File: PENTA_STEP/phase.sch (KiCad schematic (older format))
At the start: 12 parts, among them Q1 BUK9K45-100E,115, Q2 BUK9K45-100E,115

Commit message: V1 layout nearing completion
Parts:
- C27, C28, C29: footprint Capacitor_SMD:C_0603_1608Metric -> Capacitor_SMD:C_0603_1608Metric_Pad1.05x0.95mm_HandSolder
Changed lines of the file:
@@
 AR Path="/5F24B60D/5E4B900F/5E30367B" Ref="Q17"  Part="1"
 AR Path="/5F24B60D/5E4B9032/5E30367B" Ref="Q19"  Part="1"
-F 0 "Q19" H 5400 3000 50  0000 L CNN
+F 0 "Q1" H 5400 3000 50  0000 L CNN
 F 1 "BUK9K45-100E,115" H 5487 2905 50  0001 L CNN
 F 2 "CUSTOM_FP:TRANS_BUK7K12-60EX" H 5400 2875 50  0001 L CIN
@@
 AR Path="/5F24B60D/5E4B900F/5E303682" Ref="Q18"  Part="1"
 AR Path="/5F24B60D/5E4B9032/5E303682" Ref="Q20"  Part="1"
-F 0 "Q20" H 6300 3000 50  0000 L CNN
+F 0 "Q2" H 6300 3000 50  0000 L CNN
 F 1 "BUK9K45-100E,115" H 6388 2905 50  0001 L CNN
 F 2 "CUSTOM_FP:TRANS_BUK7K12-60EX" H 6300 2875 50  0001 L CIN
@@
 AR Path="/5F24B60D/5E4B900F/5E303689" Ref="Q17"  Part="2"
 AR Path="/5F24B60D/5E4B9032/5E303689" Ref="Q19"  Part="2"
-F 0 "Q19" H 5400 4250 50  0000 L CNN
+F 0 "Q1" H 5400 4250 50  0000 L CNN
 F 1 "BUK9K45-100E,115" H 5487 4155 50  0001 L CNN
 F 2 "CUSTOM_FP:TRANS_BUK7K12-60EX" H 5400 4125 50  0001 L CIN
@@
 AR Path="/5F24B60D/5E4B900F/5E303690" Ref="Q18"  Part="2"
 AR Path="/5F24B60D/5E4B9032/5E303690" Ref="Q20"  Part="2"
-F 0 "Q20" H 6300 4250 50  0000 L CNN
+F 0 "Q2" H 6300 4250 50  0000 L CNN
 F 1 "BUK9K45-100E,115" H 6388 4155 50  0001 L CNN
 F 2 "CUSTOM:TRANS_BUK7K12-60EX" H 6300 4125 50  0001 L CIN
@@
 AR Path="/5F24B60D/5E4B900F/5E303697" Ref="#PWR0109"  Part="1"
 AR Path="/5F24B60D/5E4B9032/5E303697" Ref="#PWR0111"  Part="1"
-F 0 "#PWR0111" H 5650 4950 50  0001 C CNN
+F 0 "#PWR043" H 5650 4950 50  0001 C CNN
 F 1 "GND" H 5650 5100 50  0000 C TNN
 F 2 "" H 5650 5200 50  0001 C CNN
@@
 AR Path="/5F24B60D/5E4B900F/5E30369F" Ref="R17"  Part="1"
 AR Path="/5F24B60D/5E4B9032/5E30369F" Ref="R24"  Part="1"
-F 0 "R24" V 5550 4850 50  0000 C CNN
+F 0 "R95" V 5550 4850 50  0000 C CNN
 F 1 "0R022" V 5750 4850 50  0000 C CNN
 F 2 "CUSTOM_FP:WSH2818R0500FEA" V 5580 4850 50  0001 C CNN
@@
 AR Path="/5F24B60D/5E4B900F/5E3036A9" Ref="R14"  Part="1"
 AR Path="/5F24B60D/5E4B9032/5E3036A9" Ref="R21"  Part="1"
-F 0 "R21" V 4700 4200 50  0000 C CNN
+F 0 "R92" V 4700 4200 50  0000 C CNN
 F 1 "22R" V 4900 4200 50  0000 C CNN
 F 2 "Resistor_SMD:R_0603_1608Metric_Pad1.05x0.95mm_HandSolder" V 4730 4200 50  0001 C CNN
@@
 AR Path="/5F24B60D/5E4B900F/5E3036B3" Ref="R19"  Part="1"
 AR Path="/5F24B60D/5E4B9032/5E3036B3" Ref="R26"  Part="1"
-F 0 "R26" V 6400 4200 50  0000 C CNN
+F 0 "R97" V 6400 4200 50  0000 C CNN
 F 1 "22R" V 6600 4200 50  0000 C CNN
 F 2 "Resistor_SMD:R_0603_1608Metric_Pad1.05x0.95mm_HandSolder" V 6430 4200 50  0001 C CNN
@@
 AR Path="/5F24B60D/5E4B900F/5E3036BD" Ref="R18"  Part="1"
 AR Path="/5F24B60D/5E4B9032/5E3036BD" Ref="R25"  Part="1"
-F 0 "R25" V 6400 2950 50  0000 C CNN
+F 0 "R96" V 6400 2950 50  0000 C CNN
 F 1 "22R" V 6600 2950 50  0000 C CNN
 F 2 "Resistor_SMD:R_0603_1608Metric_Pad1.05x0.95mm_HandSolder" V 6430 2950 50  0001 C CNN
@@
 AR Path="/5F24B60D/5E4B900F/5E3036C7" Ref="R13"  Part="1"
 AR Path="/5F24B60D/5E4B9032/5E3036C7" Ref="R20"  Part="1"
-F 0 "R20" V 4700 2950 50  0000 C CNN
+F 0 "R91" V 4700 2950 50  0000 C CNN
 F 1 "22R" V 4900 2950 50  0000 C CNN
 F 2 "Resistor_SMD:R_0603_1608Metric_Pad1.05x0.95mm_HandSolder" V 4730 2950 50  0001 C CNN
@@
 AR Path="/5F24B60D/5E4B900F/5E3036D1" Ref="R15"  Part="1"
 AR Path="/5F24B60D/5E4B9032/5E3036D1" Ref="R22"  Part="1"
-F 0 "R22" V 5000 4650 50  0000 C CNN
+F 0 "R93" V 5000 4650 50  0000 C CNN
 F 1 "47R" V 5200 4650 50  0000 C CNN
 F 2 "Resistor_SMD:R_0603_1608Metric_Pad1.05x0.95mm_HandSolder" V 5030 4650 50  0001 C CNN
@@
 AR Path="/5F24B60D/5E4B900F/5E3036DB" Ref="R16"  Part="1"
 AR Path="/5F24B60D/5E4B9032/5E3036DB" Ref="R23"  Part="1"
-F 0 "R23" V 5000 5050 50  0000 C CNN
+F 0 "R94" V 5000 5050 50  0000 C CNN
 F 1 "47R" V 5200 5050 50  0000 C CNN
 F 2 "Resistor_SMD:R_0603_1608Metric_Pad1.05x0.95mm_HandSolder" V 5030 5050 50  0001 C CNN
@@
 AR Path="/5F24B60D/5E4B900F/5E3036E5" Ref="C97"  Part="1"
 AR Path="/5F24B60D/5E4B9032/5E3036E5" Ref="C100"  Part="1"
-F 0 "C100" H 6265 2346 50  0000 L CNN
+F 0 "C29" H 6265 2346 50  0000 L CNN
 F 1 "470n" H 6265 2255 50  0000 L CNN
-F 2 "Capacitor_SMD:C_0603_1608Metric" H 6188 2150 50  0001 C CNN
+F 2 "Capacitor_SMD:C_0603_1608Metric_Pad1.05x0.95mm_HandSolder" H 6188 2150 50  0001 C CNN
 F 3 "~" H 6150 2300 50  0001 C CNN
 F 4 "885012106008" H 6150 2300 50  0001 C CNN "MPN"
@@
 AR Path="/5F24B60D/5E4B900F/5E3036EF" Ref="C95"  Part="1"
 AR Path="/5F24B60D/5E4B9032/5E3036EF" Ref="C98"  Part="1"
-F 0 "C98" V 5000 3450 50  0000 L BNN
+F 0 "C27" V 5000 3450 50  0000 L BNN
 F 1 "220n" V 5000 3350 50  0000 R BNN
-F 2 "Capacitor_SMD:C_0603_1608Metric" H 5038 3250 50  0001 C CNN
+F 2 "Capacitor_SMD:C_0603_1608Metric_Pad1.05x0.95mm_HandSolder" H 5038 3250 50  0001 C CNN
 F 3 "~" H 5000 3400 50  0001 C CNN
 F 4 "CL10F224ZB8NNNC" H 5000 3400 50  0001 C CNN "MPN"
@@
 AR Path="/5F24B60D/5E4B900F/5E303702" Ref="C96"  Part="1"
 AR Path="/5F24B60D/5E4B9032/5E303702" Ref="C99"  Part="1"
-F 0 "C99" V 5000 3650 50  0000 L BNN
+F 0 "C28" V 5000 3650 50  0000 L BNN
 F 1 "220n" V 5000 3550 50  0000 R BNN
-F 2 "Capacitor_SMD:C_0603_1608Metric" H 5038 3450 50  0001 C CNN
+F 2 "Capacitor_SMD:C_0603_1608Metric_Pad1.05x0.95mm_HandSolder" H 5038 3450 50  0001 C CNN
 F 3 "~" H 5000 3600 50  0001 C CNN
 F 4 "CL10F224ZB8NNNC" H 5000 3600 50  0001 C CNN "MPN"
@@
 AR Path="/5F24B60D/5E4B900F/5E303736" Ref="#PWR0110"  Part="1"
 AR Path="/5F24B60D/5E4B9032/5E303736" Ref="#PWR0112"  Part="1"
-F 0 "#PWR0112" H 6150 2250 50  0001 C CNN
+F 0 "#PWR044" H 6150 2250 50  0001 C CNN
 F 1 "GND" H 6150 2400 50  0000 C TNN
 F 2 "" H 6150 2500 50  0001 C CNN

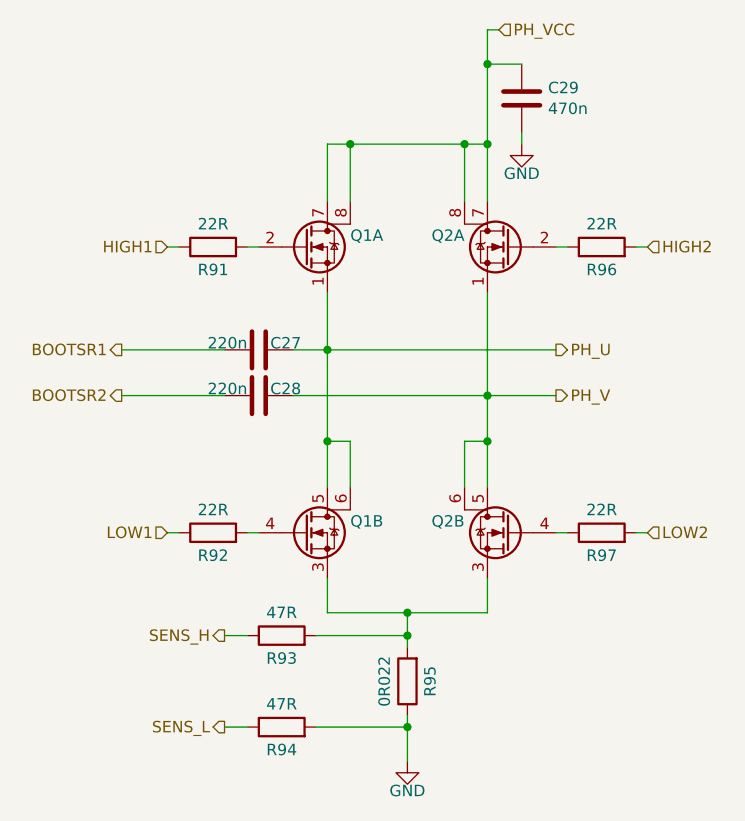
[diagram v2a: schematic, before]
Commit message: Added two FET-controlled outputs to the board
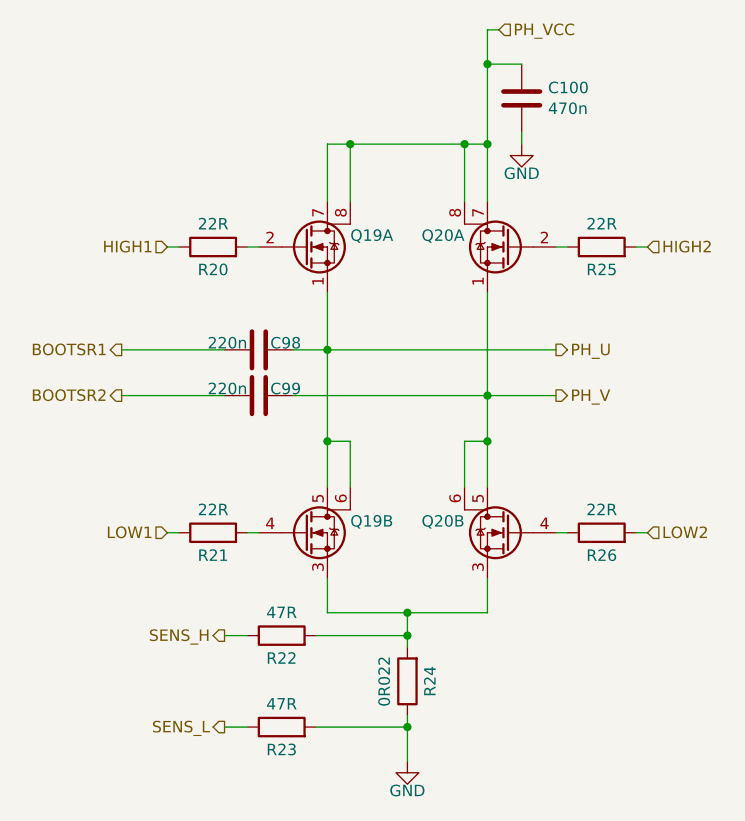
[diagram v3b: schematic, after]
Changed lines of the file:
@@
 AR Path="/5F24B60D/5E4B900F/5E30367B" Ref="Q17"  Part="1"
 AR Path="/5F24B60D/5E4B9032/5E30367B" Ref="Q19"  Part="1"
-F 0 "Q1" H 5400 3000 50  0000 L CNN
+F 0 "Q19" H 5400 3000 50  0000 L CNN
 F 1 "BUK9K45-100E,115" H 5487 2905 50  0001 L CNN
 F 2 "CUSTOM_FP:TRANS_BUK7K12-60EX" H 5400 2875 50  0001 L CIN
@@
 AR Path="/5F24B60D/5E4B900F/5E303682" Ref="Q18"  Part="1"
 AR Path="/5F24B60D/5E4B9032/5E303682" Ref="Q20"  Part="1"
-F 0 "Q2" H 6300 3000 50  0000 L CNN
+F 0 "Q20" H 6300 3000 50  0000 L CNN
 F 1 "BUK9K45-100E,115" H 6388 2905 50  0001 L CNN
 F 2 "CUSTOM_FP:TRANS_BUK7K12-60EX" H 6300 2875 50  0001 L CIN
@@
 AR Path="/5F24B60D/5E4B900F/5E303689" Ref="Q17"  Part="2"
 AR Path="/5F24B60D/5E4B9032/5E303689" Ref="Q19"  Part="2"
-F 0 "Q1" H 5400 4250 50  0000 L CNN
+F 0 "Q19" H 5400 4250 50  0000 L CNN
 F 1 "BUK9K45-100E,115" H 5487 4155 50  0001 L CNN
 F 2 "CUSTOM_FP:TRANS_BUK7K12-60EX" H 5400 4125 50  0001 L CIN
@@
 AR Path="/5F24B60D/5E4B900F/5E303690" Ref="Q18"  Part="2"
 AR Path="/5F24B60D/5E4B9032/5E303690" Ref="Q20"  Part="2"
-F 0 "Q2" H 6300 4250 50  0000 L CNN
+F 0 "Q20" H 6300 4250 50  0000 L CNN
 F 1 "BUK9K45-100E,115" H 6388 4155 50  0001 L CNN
 F 2 "CUSTOM:TRANS_BUK7K12-60EX" H 6300 4125 50  0001 L CIN
@@
 AR Path="/5F24B60D/5E4B900F/5E303697" Ref="#PWR0109"  Part="1"
 AR Path="/5F24B60D/5E4B9032/5E303697" Ref="#PWR0111"  Part="1"
-F 0 "#PWR043" H 5650 4950 50  0001 C CNN
+F 0 "#PWR0111" H 5650 4950 50  0001 C CNN
 F 1 "GND" H 5650 5100 50  0000 C TNN
 F 2 "" H 5650 5200 50  0001 C CNN
@@
 AR Path="/5F24B60D/5E4B900F/5E30369F" Ref="R17"  Part="1"
 AR Path="/5F24B60D/5E4B9032/5E30369F" Ref="R24"  Part="1"
-F 0 "R95" V 5550 4850 50  0000 C CNN
+F 0 "R24" V 5550 4850 50  0000 C CNN
 F 1 "0R022" V 5750 4850 50  0000 C CNN
 F 2 "CUSTOM_FP:WSH2818R0500FEA" V 5580 4850 50  0001 C CNN
@@
 AR Path="/5F24B60D/5E4B900F/5E3036A9" Ref="R14"  Part="1"
 AR Path="/5F24B60D/5E4B9032/5E3036A9" Ref="R21"  Part="1"
-F 0 "R92" V 4700 4200 50  0000 C CNN
+F 0 "R21" V 4700 4200 50  0000 C CNN
 F 1 "22R" V 4900 4200 50  0000 C CNN
 F 2 "Resistor_SMD:R_0603_1608Metric_Pad1.05x0.95mm_HandSolder" V 4730 4200 50  0001 C CNN
@@
 AR Path="/5F24B60D/5E4B900F/5E3036B3" Ref="R19"  Part="1"
 AR Path="/5F24B60D/5E4B9032/5E3036B3" Ref="R26"  Part="1"
-F 0 "R97" V 6400 4200 50  0000 C CNN
+F 0 "R26" V 6400 4200 50  0000 C CNN
 F 1 "22R" V 6600 4200 50  0000 C CNN
 F 2 "Resistor_SMD:R_0603_1608Metric_Pad1.05x0.95mm_HandSolder" V 6430 4200 50  0001 C CNN
@@
 AR Path="/5F24B60D/5E4B900F/5E3036BD" Ref="R18"  Part="1"
 AR Path="/5F24B60D/5E4B9032/5E3036BD" Ref="R25"  Part="1"
-F 0 "R96" V 6400 2950 50  0000 C CNN
+F 0 "R25" V 6400 2950 50  0000 C CNN
 F 1 "22R" V 6600 2950 50  0000 C CNN
 F 2 "Resistor_SMD:R_0603_1608Metric_Pad1.05x0.95mm_HandSolder" V 6430 2950 50  0001 C CNN
@@
 AR Path="/5F24B60D/5E4B900F/5E3036C7" Ref="R13"  Part="1"
 AR Path="/5F24B60D/5E4B9032/5E3036C7" Ref="R20"  Part="1"
-F 0 "R91" V 4700 2950 50  0000 C CNN
+F 0 "R20" V 4700 2950 50  0000 C CNN
 F 1 "22R" V 4900 2950 50  0000 C CNN
 F 2 "Resistor_SMD:R_0603_1608Metric_Pad1.05x0.95mm_HandSolder" V 4730 2950 50  0001 C CNN
@@
 AR Path="/5F24B60D/5E4B900F/5E3036D1" Ref="R15"  Part="1"
 AR Path="/5F24B60D/5E4B9032/5E3036D1" Ref="R22"  Part="1"
-F 0 "R93" V 5000 4650 50  0000 C CNN
+F 0 "R22" V 5000 4650 50  0000 C CNN
 F 1 "47R" V 5200 4650 50  0000 C CNN
 F 2 "Resistor_SMD:R_0603_1608Metric_Pad1.05x0.95mm_HandSolder" V 5030 4650 50  0001 C CNN
@@
 AR Path="/5F24B60D/5E4B900F/5E3036DB" Ref="R16"  Part="1"
 AR Path="/5F24B60D/5E4B9032/5E3036DB" Ref="R23"  Part="1"
-F 0 "R94" V 5000 5050 50  0000 C CNN
+F 0 "R23" V 5000 5050 50  0000 C CNN
 F 1 "47R" V 5200 5050 50  0000 C CNN
 F 2 "Resistor_SMD:R_0603_1608Metric_Pad1.05x0.95mm_HandSolder" V 5030 5050 50  0001 C CNN
@@
 AR Path="/5F24B60D/5E4B900F/5E3036E5" Ref="C97"  Part="1"
 AR Path="/5F24B60D/5E4B9032/5E3036E5" Ref="C100"  Part="1"
-F 0 "C29" H 6265 2346 50  0000 L CNN
+F 0 "C100" H 6265 2346 50  0000 L CNN
 F 1 "470n" H 6265 2255 50  0000 L CNN
 F 2 "Capacitor_SMD:C_0603_1608Metric_Pad1.05x0.95mm_HandSolder" H 6188 2150 50  0001 C CNN
@@
 AR Path="/5F24B60D/5E4B900F/5E3036EF" Ref="C95"  Part="1"
 AR Path="/5F24B60D/5E4B9032/5E3036EF" Ref="C98"  Part="1"
-F 0 "C27" V 5000 3450 50  0000 L BNN
+F 0 "C98" V 5000 3450 50  0000 L BNN
 F 1 "220n" V 5000 3350 50  0000 R BNN
 F 2 "Capacitor_SMD:C_0603_1608Metric_Pad1.05x0.95mm_HandSolder" H 5038 3250 50  0001 C CNN
@@
 AR Path="/5F24B60D/5E4B900F/5E303702" Ref="C96"  Part="1"
 AR Path="/5F24B60D/5E4B9032/5E303702" Ref="C99"  Part="1"
-F 0 "C28" V 5000 3650 50  0000 L BNN
+F 0 "C99" V 5000 3650 50  0000 L BNN
 F 1 "220n" V 5000 3550 50  0000 R BNN
 F 2 "Capacitor_SMD:C_0603_1608Metric_Pad1.05x0.95mm_HandSolder" H 5038 3450 50  0001 C CNN
@@
 AR Path="/5F24B60D/5E4B900F/5E303736" Ref="#PWR0110"  Part="1"
 AR Path="/5F24B60D/5E4B9032/5E303736" Ref="#PWR0112"  Part="1"
-F 0 "#PWR044" H 6150 2250 50  0001 C CNN
+F 0 "#PWR0112" H 6150 2250 50  0001 C CNN
 F 1 "GND" H 6150 2400 50  0000 C TNN
 F 2 "" H 6150 2500 50  0001 C CNN

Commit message: majority routed, eliminated ATTINY coprocessor
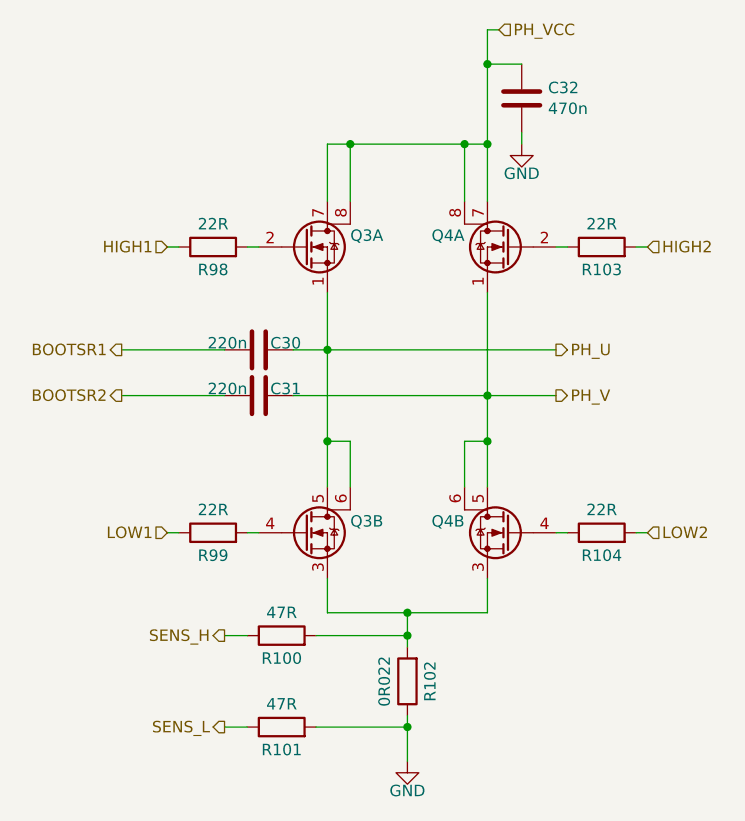
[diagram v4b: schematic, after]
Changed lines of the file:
@@
 AR Path="/5F24B60D/5E4B900F/5E30367B" Ref="Q17"  Part="1"
 AR Path="/5F24B60D/5E4B9032/5E30367B" Ref="Q19"  Part="1"
-F 0 "Q19" H 5400 3000 50  0000 L CNN
+F 0 "Q3" H 5400 3000 50  0000 L CNN
 F 1 "BUK9K45-100E,115" H 5487 2905 50  0001 L CNN
 F 2 "CUSTOM_FP:TRANS_BUK7K12-60EX" H 5400 2875 50  0001 L CIN
@@
 AR Path="/5F24B60D/5E4B900F/5E303682" Ref="Q18"  Part="1"
 AR Path="/5F24B60D/5E4B9032/5E303682" Ref="Q20"  Part="1"
-F 0 "Q20" H 6300 3000 50  0000 L CNN
+F 0 "Q4" H 6300 3000 50  0000 L CNN
 F 1 "BUK9K45-100E,115" H 6388 2905 50  0001 L CNN
 F 2 "CUSTOM_FP:TRANS_BUK7K12-60EX" H 6300 2875 50  0001 L CIN
@@
 AR Path="/5F24B60D/5E4B900F/5E303689" Ref="Q17"  Part="2"
 AR Path="/5F24B60D/5E4B9032/5E303689" Ref="Q19"  Part="2"
-F 0 "Q19" H 5400 4250 50  0000 L CNN
+F 0 "Q3" H 5400 4250 50  0000 L CNN
 F 1 "BUK9K45-100E,115" H 5487 4155 50  0001 L CNN
 F 2 "CUSTOM_FP:TRANS_BUK7K12-60EX" H 5400 4125 50  0001 L CIN
@@
 AR Path="/5F24B60D/5E4B900F/5E303690" Ref="Q18"  Part="2"
 AR Path="/5F24B60D/5E4B9032/5E303690" Ref="Q20"  Part="2"
-F 0 "Q20" H 6300 4250 50  0000 L CNN
+F 0 "Q4" H 6300 4250 50  0000 L CNN
 F 1 "BUK9K45-100E,115" H 6388 4155 50  0001 L CNN
 F 2 "CUSTOM:TRANS_BUK7K12-60EX" H 6300 4125 50  0001 L CIN
@@
 AR Path="/5F24B60D/5E4B900F/5E303697" Ref="#PWR0109"  Part="1"
 AR Path="/5F24B60D/5E4B9032/5E303697" Ref="#PWR0111"  Part="1"
-F 0 "#PWR0111" H 5650 4950 50  0001 C CNN
+F 0 "#PWR045" H 5650 4950 50  0001 C CNN
 F 1 "GND" H 5650 5100 50  0000 C TNN
 F 2 "" H 5650 5200 50  0001 C CNN
@@
 AR Path="/5F24B60D/5E4B900F/5E30369F" Ref="R17"  Part="1"
 AR Path="/5F24B60D/5E4B9032/5E30369F" Ref="R24"  Part="1"
-F 0 "R24" V 5550 4850 50  0000 C CNN
+F 0 "R102" V 5550 4850 50  0000 C CNN
 F 1 "0R022" V 5750 4850 50  0000 C CNN
 F 2 "CUSTOM_FP:WSH2818R0500FEA" V 5580 4850 50  0001 C CNN
@@
 AR Path="/5F24B60D/5E4B900F/5E3036A9" Ref="R14"  Part="1"
 AR Path="/5F24B60D/5E4B9032/5E3036A9" Ref="R21"  Part="1"
-F 0 "R21" V 4700 4200 50  0000 C CNN
+F 0 "R99" V 4700 4200 50  0000 C CNN
 F 1 "22R" V 4900 4200 50  0000 C CNN
 F 2 "Resistor_SMD:R_0603_1608Metric_Pad1.05x0.95mm_HandSolder" V 4730 4200 50  0001 C CNN
@@
 AR Path="/5F24B60D/5E4B900F/5E3036B3" Ref="R19"  Part="1"
 AR Path="/5F24B60D/5E4B9032/5E3036B3" Ref="R26"  Part="1"
-F 0 "R26" V 6400 4200 50  0000 C CNN
+F 0 "R104" V 6400 4200 50  0000 C CNN
 F 1 "22R" V 6600 4200 50  0000 C CNN
 F 2 "Resistor_SMD:R_0603_1608Metric_Pad1.05x0.95mm_HandSolder" V 6430 4200 50  0001 C CNN
@@
 AR Path="/5F24B60D/5E4B900F/5E3036BD" Ref="R18"  Part="1"
 AR Path="/5F24B60D/5E4B9032/5E3036BD" Ref="R25"  Part="1"
-F 0 "R25" V 6400 2950 50  0000 C CNN
+F 0 "R103" V 6400 2950 50  0000 C CNN
 F 1 "22R" V 6600 2950 50  0000 C CNN
 F 2 "Resistor_SMD:R_0603_1608Metric_Pad1.05x0.95mm_HandSolder" V 6430 2950 50  0001 C CNN
@@
 AR Path="/5F24B60D/5E4B900F/5E3036C7" Ref="R13"  Part="1"
 AR Path="/5F24B60D/5E4B9032/5E3036C7" Ref="R20"  Part="1"
-F 0 "R20" V 4700 2950 50  0000 C CNN
+F 0 "R98" V 4700 2950 50  0000 C CNN
 F 1 "22R" V 4900 2950 50  0000 C CNN
 F 2 "Resistor_SMD:R_0603_1608Metric_Pad1.05x0.95mm_HandSolder" V 4730 2950 50  0001 C CNN
@@
 AR Path="/5F24B60D/5E4B900F/5E3036D1" Ref="R15"  Part="1"
 AR Path="/5F24B60D/5E4B9032/5E3036D1" Ref="R22"  Part="1"
-F 0 "R22" V 5000 4650 50  0000 C CNN
+F 0 "R100" V 5000 4650 50  0000 C CNN
 F 1 "47R" V 5200 4650 50  0000 C CNN
 F 2 "Resistor_SMD:R_0603_1608Metric_Pad1.05x0.95mm_HandSolder" V 5030 4650 50  0001 C CNN
@@
 AR Path="/5F24B60D/5E4B900F/5E3036DB" Ref="R16"  Part="1"
 AR Path="/5F24B60D/5E4B9032/5E3036DB" Ref="R23"  Part="1"
-F 0 "R23" V 5000 5050 50  0000 C CNN
+F 0 "R101" V 5000 5050 50  0000 C CNN
 F 1 "47R" V 5200 5050 50  0000 C CNN
 F 2 "Resistor_SMD:R_0603_1608Metric_Pad1.05x0.95mm_HandSolder" V 5030 5050 50  0001 C CNN
@@
 AR Path="/5F24B60D/5E4B900F/5E3036E5" Ref="C97"  Part="1"
 AR Path="/5F24B60D/5E4B9032/5E3036E5" Ref="C100"  Part="1"
-F 0 "C100" H 6265 2346 50  0000 L CNN
+F 0 "C32" H 6265 2346 50  0000 L CNN
 F 1 "470n" H 6265 2255 50  0000 L CNN
 F 2 "Capacitor_SMD:C_0603_1608Metric_Pad1.05x0.95mm_HandSolder" H 6188 2150 50  0001 C CNN
@@
 AR Path="/5F24B60D/5E4B900F/5E3036EF" Ref="C95"  Part="1"
 AR Path="/5F24B60D/5E4B9032/5E3036EF" Ref="C98"  Part="1"
-F 0 "C98" V 5000 3450 50  0000 L BNN
+F 0 "C30" V 5000 3450 50  0000 L BNN
 F 1 "220n" V 5000 3350 50  0000 R BNN
 F 2 "Capacitor_SMD:C_0603_1608Metric_Pad1.05x0.95mm_HandSolder" H 5038 3250 50  0001 C CNN
@@
 AR Path="/5F24B60D/5E4B900F/5E303702" Ref="C96"  Part="1"
 AR Path="/5F24B60D/5E4B9032/5E303702" Ref="C99"  Part="1"
-F 0 "C99" V 5000 3650 50  0000 L BNN
+F 0 "C31" V 5000 3650 50  0000 L BNN
 F 1 "220n" V 5000 3550 50  0000 R BNN
 F 2 "Capacitor_SMD:C_0603_1608Metric_Pad1.05x0.95mm_HandSolder" H 5038 3450 50  0001 C CNN
@@
 AR Path="/5F24B60D/5E4B900F/5E303736" Ref="#PWR0110"  Part="1"
 AR Path="/5F24B60D/5E4B9032/5E303736" Ref="#PWR0112"  Part="1"
-F 0 "#PWR0112" H 6150 2250 50  0001 C CNN
+F 0 "#PWR046" H 6150 2250 50  0001 C CNN
 F 1 "GND" H 6150 2400 50  0000 C TNN
 F 2 "" H 6150 2500 50  0001 C CNN
